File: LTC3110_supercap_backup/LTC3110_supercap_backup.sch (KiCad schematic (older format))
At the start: 28 parts

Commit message: Updated layout to include more net lables, ports, connectors
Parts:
- added P?: CONN_01X02, symbol CONN_01X02
- added P?: CONN_01X05, symbol CONN_01X05
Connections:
- net labels added: CAPOK, CAP_OK, DIR, FB, FBVCAP, MODE, RUN, VCAP, V_MID, V_SOLAR
- wire segments 87 -> 94
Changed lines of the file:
@@
 	4300 5250 4450 5250
 Wire Wire Line
-	2750 4700 2750 4650
+	2750 4650 2750 4700
 Wire Wire Line
 	3500 7200 7550 7200
@@
 $EndComp
 Wire Wire Line
-	8450 2650 8450 3150
-Wire Wire Line
-	8750 2900 8750 3150
-Wire Wire Line
 	8700 3150 8800 3150
 Connection ~ 8750 3150
@@
 	1    0    0    -1
 $EndComp
-Connection ~ 8450 2900
 $Comp
 L GND #PWR?
@@
 	1    0    0    -1
 $EndComp
-Wire Wire Line
-	8750 2900 11500 2900
 $Comp
 L C C?
@@
 	10650 4650 11300 4650
 Connection ~ 10700 2900
-Text GLabel 11500 2900 2    60   Input ~ 0
+Text GLabel 11300 2900 2    60   Input ~ 0
 V_SYS
 Text GLabel 11300 4650 2    60   Input ~ 0
 CAP_LOW
+Text GLabel 2500 4000 0    60   Input ~ 0
+V_SOLAR
+Wire Wire Line
+	2500 4000 2750 4000
+Connection ~ 2750 4000
+Text GLabel 2500 4650 0    60   Input ~ 0
+GND
+Wire Wire Line
+	2500 4650 2750 4650
+Text GLabel 11300 5200 2    60   Input ~ 0
+CAP_OK
+Connection ~ 9350 5200
+Wire Wire Line
+	11300 5200 9350 5200
+Wire Wire Line
+	8750 2900 11300 2900
+Wire Wire Line
+	8450 2650 8450 3150
+Connection ~ 8450 2900
+Wire Wire Line
+	8750 2900 8750 3150
+Text Label 5900 5250 0    60   ~ 0
+RUN
+Text Label 7350 7900 0    60   ~ 0
+MODE
+Text Label 9850 5200 0    60   ~ 0
+CAPOK
+Text Label 9250 4650 0    60   ~ 0
+DIR
+Text Label 9250 4300 0    60   ~ 0
+FB
+Text Label 6900 3150 0    60   ~ 0
+FBVCAP
+Text Label 5500 3650 0    60   ~ 0
+VCAP
+Text Label 5850 4800 0    60   ~ 0
+V_MID
+Text Label 2750 3550 0    60   ~ 0
+V_SOLAR
+$Comp
+L CONN_01X02 P?
+U 1 1 57C924FF
+P 1400 4300
+F 0 "P?" H 1400 4450 50  0000 C CNN
+F 1 "CONN_01X02" V 1500 4300 50  0000 C CNN
+F 2 "" H 1400 4300 50  0000 C CNN
+F 3 "" H 1400 4300 50  0000 C CNN
+	1    1400 4300
+	-1   0    0    -1
+$EndComp
+Connection ~ 2750 3850
+Wire Wire Line
+	1600 4350 2550 4350
+Wire Wire Line
+	2550 4350 2550 4650
+Connection ~ 2550 4650
+Wire Wire Line
+	1600 4250 1600 4100
+Wire Wire Line
+	1600 4100 2750 4100
+Connection ~ 2750 4100
+$Comp
+L CONN_01X05 P?
+U 1 1 57C92BCD
+P 13500 3800
+F 0 "P?" H 13500 4100 50  0000 C CNN
+F 1 "CONN_01X05" V 13600 3800 50  0000 C CNN
+F 2 "" H 13500 3800 50  0000 C CNN
+F 3 "" H 13500 3800 50  0000 C CNN
+	1    13500 3800
+	1    0    0    -1
+$EndComp
+Text GLabel 13300 3600 0    60   Input ~ 0
+V_SYS
+Text GLabel 13300 3700 0    60   Input ~ 0
+CAP_LOW
+Text GLabel 13300 3800 0    60   Input ~ 0
+CAP_OK
+Text GLabel 13300 4000 0    60   Input ~ 0
+GND
 $EndSCHEMATC

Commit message: Schematic tweaked and annotated, looking good, time for footprint matching and layout.
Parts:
- removed BT?: Solar Panel, symbol Battery
- removed P?: CONN_01X05, symbol CONN_01X05
- added P?: CONN_01X02, symbol CONN_01X02
- added P?: CONN_01X05, symbol CONN_01X05
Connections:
- net labels added: !CHRG
- wire segments 94 -> 99
- no-connect marks 4 -> 3
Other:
- note added: "Drawn by: Matthew Valancy\nBased on: LTC3110 datasheet page 32"
- moved on the sheet: P?
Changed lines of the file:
@@
-$EndComp
-$Comp
-L Battery BT?
-U 1 1 57C7BCD4
-P 2750 4500
-F 0 "BT?" H 2850 4550 50  0000 L CNN
-F 1 "Solar Panel" H 2850 4450 50  0000 L CNN
-F 2 "" V 2750 4540 50  0000 C CNN
-F 3 "" V 2750 4540 50  0000 C CNN
-	1    2750 4500
-	1    0    0    -1
 $EndComp
 $Comp
@@
 $EndComp
 Wire Wire Line
-	3050 4200 2750 4200
-Wire Wire Line
-	2750 3550 2750 4350
+	2750 4200 3050 4200
 Wire Wire Line
 	3500 4200 3350 4200
@@
 	4300 5250 4450 5250
 Wire Wire Line
-	2750 4650 2750 4700
+	2750 4400 2750 4700
 Wire Wire Line
 	3500 7200 7550 7200
@@
 	1    0    0    -1
 $EndComp
-NoConn ~ 9100 4900
 $Comp
 L R R?
@@
 L GND #PWR?
 U 1 1 57C8193E
-P 9750 5000
-F 0 "#PWR?" H 9750 4750 50  0001 C CNN
-F 1 "GND" H 9650 5050 50  0001 C CNN
-F 2 "" H 9750 5000 50  0000 C CNN
-F 3 "" H 9750 5000 50  0000 C CNN
-	1    9750 5000
-	1    0    0    -1
-$EndComp
-Wire Wire Line
-	9750 5000 9750 4950
+P 9750 4950
+F 0 "#PWR?" H 9750 4700 50  0001 C CNN
+F 1 "GND" H 9650 5000 50  0001 C CNN
+F 2 "" H 9750 4950 50  0000 C CNN
+F 3 "" H 9750 4950 50  0000 C CNN
+	1    9750 4950
+	1    0    0    -1
+$EndComp
 Wire Wire Line
 	10150 4650 10350 4650
@@
 Text Label 6900 3150 0    60   ~ 0
 FBVCAP
-Text Label 5500 3650 0    60   ~ 0
+Text Label 5650 3650 0    60   ~ 0
 VCAP
 Text Label 5850 4800 0    60   ~ 0
@@
 L CONN_01X02 P?
 U 1 1 57C924FF
-P 1400 4300
-F 0 "P?" H 1400 4450 50  0000 C CNN
-F 1 "CONN_01X02" V 1500 4300 50  0000 C CNN
-F 2 "" H 1400 4300 50  0000 C CNN
-F 3 "" H 1400 4300 50  0000 C CNN
-	1    1400 4300
+P 2150 4350
+F 0 "P?" H 2150 4500 50  0000 C CNN
+F 1 "CONN_01X02" V 2250 4350 50  0000 C CNN
+F 2 "" H 2150 4350 50  0000 C CNN
+F 3 "" H 2150 4350 50  0000 C CNN
+	1    2150 4350
 	-1   0    0    -1
 $EndComp
-Connection ~ 2750 3850
-Wire Wire Line
-	1600 4350 2550 4350
-Wire Wire Line
-	2550 4350 2550 4650
-Connection ~ 2550 4650
-Wire Wire Line
-	1600 4250 1600 4100
-Wire Wire Line
-	1600 4100 2750 4100
-Connection ~ 2750 4100
+Text GLabel 13300 3600 0    60   Input ~ 0
+V_SYS
+Text GLabel 13300 3800 0    60   Input ~ 0
+CAP_LOW
+Text GLabel 13300 3900 0    60   Input ~ 0
+CAP_OK
+Wire Wire Line
+	2750 3550 2750 4300
+Wire Wire Line
+	2750 4300 2350 4300
+Wire Wire Line
+	2350 4400 2750 4400
+Connection ~ 2750 4650
+Text GLabel 9100 4900 2    60   Input ~ 0
+!CHRG
+Text GLabel 13300 4000 0    60   Input ~ 0
+!CHRG
+Text GLabel 13300 3700 0    60   Input ~ 0
+GND
+$Comp
+L CONN_01X02 P?
+U 1 1 57C9525E
+P 4850 4150
+F 0 "P?" H 4850 4300 50  0000 C CNN
+F 1 "CONN_01X02" V 4950 4150 50  0000 C CNN
+F 2 "" H 4850 4150 50  0000 C CNN
+F 3 "" H 4850 4150 50  0000 C CNN
+	1    4850 4150
+	-1   0    0    -1
+$EndComp
+Wire Wire Line
+	5050 4100 5250 4100
+Wire Wire Line
+	5250 4100 5250 3800
+Wire Wire Line
+	5250 3800 5500 3800
+Connection ~ 5500 3800
+Wire Wire Line
+	5050 4200 5200 4200
+Wire Wire Line
+	5200 4200 5200 4650
+Wire Wire Line
+	5200 4650 5500 4650
+Connection ~ 5500 4650
+Wire Wire Line
+	9100 5100 10850 5100
+Wire Wire Line
+	10850 5100 10850 4650
+Connection ~ 10850 4650
 $Comp
 L CONN_01X05 P?
-U 1 1 57C92BCD
+U 1 1 57C961F0
 P 13500 3800
 F 0 "P?" H 13500 4100 50  0000 C CNN
@@
 	1    0    0    -1
 $EndComp
-Text GLabel 13300 3600 0    60   Input ~ 0
-V_SYS
-Text GLabel 13300 3700 0    60   Input ~ 0
-CAP_LOW
-Text GLabel 13300 3800 0    60   Input ~ 0
-CAP_OK
-Text GLabel 13300 4000 0    60   Input ~ 0
-GND
+Text Notes 12350 9500 0    60   ~ 0
+Drawn by: Matthew Valancy\nBased on: LTC3110 datasheet page 32
 $EndSCHEMATC

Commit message: saved project
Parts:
- gave numbers to parts that had none: 30

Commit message: Selected critical components for LTC3110 breakout, associated footprints and added necessary footprints to library, output netlist and started layout
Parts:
- removed U1: LTC2935-2, symbol LTC2935-2
- added U1: LTC2935-2-TS8, TO_SOT_Packages_SMD:SOT-23, symbol LTC2935-2-TS8
- C1, C2: footprint (none) -> MRV_TH_Passives:Cap_HB1860; MFG_PN (none) -> HB1860-2R5117-R
- C3, C4, C5, C6: footprint (none) -> Capacitors_SMD:C_0805_HandSoldering
- C7, C8: footprint (none) -> Capacitors_ThroughHole:C_Rect_L32_W15_P27; MFG_PN (none) -> UHW1E472MHD
- L1: footprint (none) -> MRV_SMD_Passives:SMD_IND_CLF7045; MFG_PN (none) -> CLF7045T-2R2N-D
- M1, M2: footprint (none) -> TO_SOT_Packages_SMD:SOT-23
- P1, P2: footprint (none) -> Pin_Headers:Pin_Header_Straight_1x02
- P3: footprint (none) -> Pin_Headers:Pin_Header_Straight_1x05
- Q1: footprint (none) -> TO_SOT_Packages_SMD:SOT-223; MFG_PN (none) -> PBSS302
- R1, R10, R11, R12, R13, R4, R5, R6, R7, R8, R9: footprint (none) -> Resistors_SMD:R_0805_HandSoldering
- R2: footprint (none) -> Resistors_SMD:R_0805_HandSoldering; MFG_PN (none) -> ERJ-6ENF1914V
- R3: footprint (none) -> Resistors_SMD:R_0805_HandSoldering; MFG_PN (none) -> CRCW0805523KFKEA
- U2: footprint (none) -> MRV_SMD_Packages:TSSOP-24

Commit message: Layout almost complete
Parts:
- U1: footprint TO_SOT_Packages_SMD:SOT-23 -> MRV_SMD_Packages:TSOT-23-8
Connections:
- wire segments 99 -> 102
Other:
- moved on the sheet: C3
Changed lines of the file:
@@
 LIBS:contrib
 LIBS:valves
-LIBS:ICs_PM
-LIBS:MF_Aesthetics
-LIBS:MF_Connectors
-LIBS:MF_Discrete_Semiconductor
-LIBS:MF_Displays
-LIBS:MF_Frequency_Control
-LIBS:MF_IC_Analog
-LIBS:MF_IC_Digital
-LIBS:MF_IC_Power
-LIBS:MF_LEDs
-LIBS:MF_Passives
-LIBS:MF_Sensors
-LIBS:MF_Switches
 LIBS:LTC3110_supercap_backup-cache
 EELAYER 25 0
@@
 L C C3
 U 1 1 57C7F46D
-P 6650 3800
-F 0 "C3" H 6675 3900 50  0000 L CNN
-F 1 "47uF" H 6675 3700 50  0000 L CNN
-F 2 "Capacitors_SMD:C_0805_HandSoldering" H 6688 3650 50  0001 C CNN
-F 3 "" H 6650 3800 50  0000 C CNN
-	1    6650 3800
+P 6650 3850
+F 0 "C3" H 6675 3950 50  0000 L CNN
+F 1 "47uF" H 6675 3750 50  0000 L CNN
+F 2 "Capacitors_SMD:C_0805_HandSoldering" H 6688 3700 50  0001 C CNN
+F 3 "" H 6650 3850 50  0000 C CNN
+	1    6650 3850
 	1    0    0    -1
 $EndComp
@@
 L GND #PWR013
 U 1 1 57C7F4EE
-P 6650 4000
-F 0 "#PWR013" H 6650 3750 50  0001 C CNN
-F 1 "GND" H 6550 4050 50  0001 C CNN
-F 2 "" H 6650 4000 50  0000 C CNN
-F 3 "" H 6650 4000 50  0000 C CNN
-	1    6650 4000
-	1    0    0    -1
-$EndComp
-Wire Wire Line
-	6650 4000 6650 3950
+P 6650 4050
+F 0 "#PWR013" H 6650 3800 50  0001 C CNN
+F 1 "GND" H 6550 4100 50  0001 C CNN
+F 2 "" H 6650 4050 50  0000 C CNN
+F 3 "" H 6650 4050 50  0000 C CNN
+	1    6650 4050
+	1    0    0    -1
+$EndComp
 $Comp
 L L_Small L1
@@
 	9750 3750 10250 3750
 Connection ~ 10250 4650
-Wire Wire Line
-	9800 2150 9800 3750
 Connection ~ 9800 2900
 Wire Wire Line
@@
 F 0 "U1" H 4750 7200 60  0000 C CNN
 F 1 "LTC2935-2-TS8" H 5050 7100 60  0000 C CNN
-F 2 "TO_SOT_Packages_SMD:SOT-23" H 4450 6100 60  0001 C CNN
+F 2 "MRV_SMD_Packages:TSOT-23-8" H 4450 6100 60  0001 C CNN
 F 3 "" H 4450 6100 60  0001 C CNN
 	1    4450 6000
 	1    0    0    -1
 $EndComp
+Wire Wire Line
+	8300 5500 8450 5500
+Wire Wire Line
+	7900 5650 8100 5650
+Wire Wire Line
+	6650 4050 6650 4000
+Wire Wire Line
+	6650 3700 6650 3650
+Connection ~ 6650 3650
+Wire Wire Line
+	9800 3750 9800 2900
+Connection ~ 9800 3750
 $EndSCHEMATC

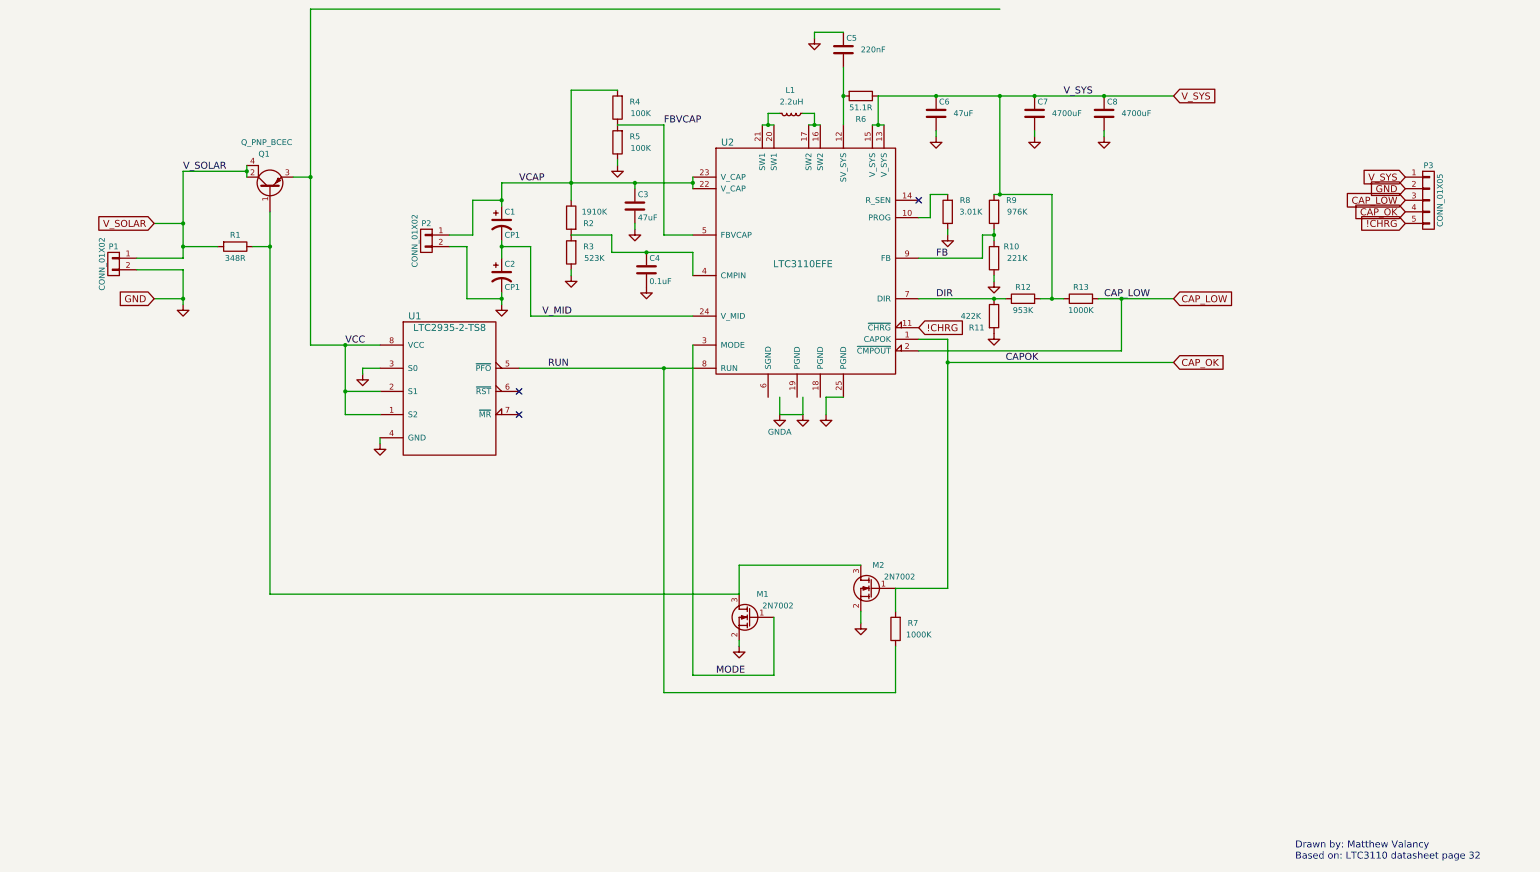
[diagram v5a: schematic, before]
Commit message: re-routed CAP_OK to avoid major ground plane division
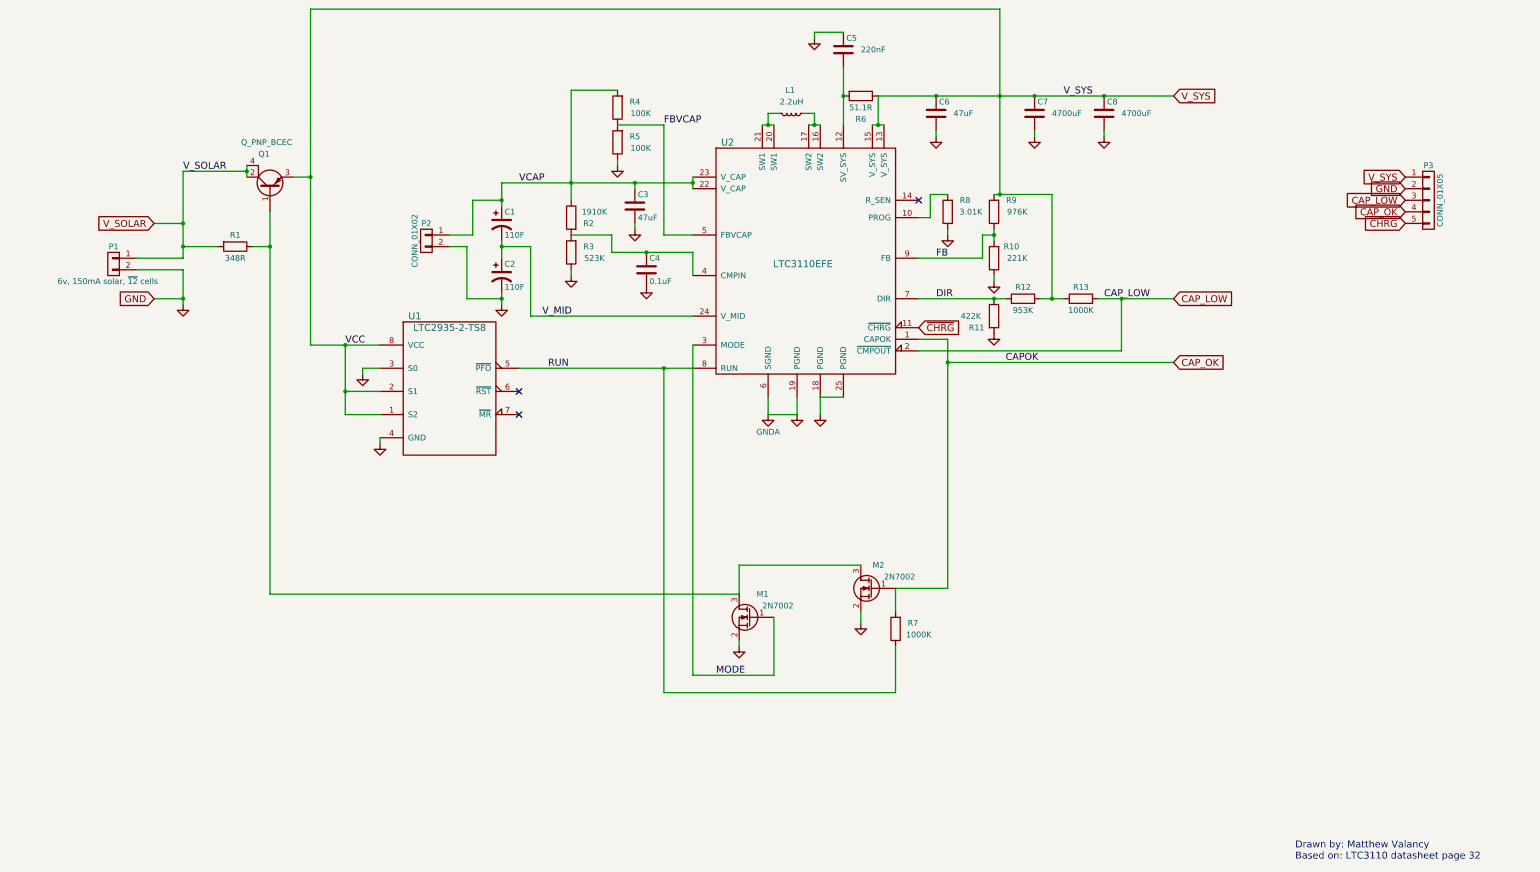
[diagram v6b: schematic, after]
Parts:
- C1, C2: value CP1 -> 110F
- P1: value CONN_01X02 -> 6v, 150mA solar, ~12 cells
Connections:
- net VCC is gone; now on net V_SYS: Q1.3 (E), U1.1 (S2), U1.2 (S1), U1.8 (VCC)
- net GND: now also U2.18 (PGND), U2.19 (PGND), U2.6 (SGND)
- net !CHRG renamed ~CHRG
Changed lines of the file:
@@
 LIBS:contrib
 LIBS:valves
+LIBS:MRV_ICs_PM
 LIBS:LTC3110_supercap_backup-cache
 EELAYER 25 0
@@
 L GNDA #PWR06
 U 1 1 57C7DBE5
-P 7900 5650
-F 0 "#PWR06" H 7900 5400 50  0001 C CNN
-F 1 "GNDA" H 7900 5500 50  0000 C CNN
-F 2 "" H 7900 5650 50  0000 C CNN
-F 3 "" H 7900 5650 50  0000 C CNN
-	1    7900 5650
+P 7800 5650
+F 0 "#PWR06" H 7800 5400 50  0001 C CNN
+F 1 "GNDA" H 7800 5500 50  0000 C CNN
+F 2 "" H 7800 5650 50  0000 C CNN
+F 3 "" H 7800 5650 50  0000 C CNN
+	1    7800 5650
 	1    0    0    -1
 $EndComp
@@
 L GND #PWR07
 U 1 1 57C7DC74
-P 8100 5650
-F 0 "#PWR07" H 8100 5400 50  0001 C CNN
-F 1 "GND" H 8000 5700 50  0001 C CNN
-F 2 "" H 8100 5650 50  0000 C CNN
-F 3 "" H 8100 5650 50  0000 C CNN
-	1    8100 5650
+P 8050 5650
+F 0 "#PWR07" H 8050 5400 50  0001 C CNN
+F 1 "GND" H 7950 5700 50  0001 C CNN
+F 2 "" H 8050 5650 50  0000 C CNN
+F 3 "" H 8050 5650 50  0000 C CNN
+	1    8050 5650
 	1    0    0    -1
 $EndComp
@@
 L GND #PWR08
 U 1 1 57C7DCF0
-P 8300 5650
-F 0 "#PWR08" H 8300 5400 50  0001 C CNN
-F 1 "GND" H 8200 5700 50  0001 C CNN
-F 2 "" H 8300 5650 50  0000 C CNN
-F 3 "" H 8300 5650 50  0000 C CNN
-	1    8300 5650
+P 8250 5650
+F 0 "#PWR08" H 8250 5400 50  0001 C CNN
+F 1 "GND" H 8150 5700 50  0001 C CNN
+F 2 "" H 8250 5650 50  0000 C CNN
+F 3 "" H 8250 5650 50  0000 C CNN
+	1    8250 5650
 	1    0    0    -1
 $EndComp
@@
 P 5500 4000
 F 0 "C1" H 5525 4100 50  0000 L CNN
-F 1 "CP1" H 5525 3900 50  0000 L CNN
+F 1 "110F" H 5525 3900 50  0000 L CNN
 F 2 "MRV_TH_Passives:Cap_HB1860" H 5500 4000 50  0001 C CNN
 F 3 "" H 5500 4000 50  0000 C CNN
@@
 P 5500 4450
 F 0 "C2" H 5525 4550 50  0000 L CNN
-F 1 "CP1" H 5525 4350 50  0000 L CNN
+F 1 "110F" H 5525 4350 50  0000 L CNN
 F 2 "MRV_TH_Passives:Cap_HB1860" H 5500 4450 50  0001 C CNN
 F 3 "" H 5500 4450 50  0000 C CNN
@@
 	3500 4200 3350 4200
 Wire Wire Line
-	3300 3500 3300 3600
+	3300 3500 3300 3550
+Wire Wire Line
+	3300 3550 3300 3600
 Wire Wire Line
 	2750 3550 3300 3550
@@
 	3700 3600 3850 3600
 Wire Wire Line
-	3850 2150 3850 5050
-Wire Wire Line
-	3850 5050 4450 5050
+	3850 2150 3850 3600
+Wire Wire Line
+	3850 3600 3850 5050
+Wire Wire Line
+	3850 5050 4150 5050
+Wire Wire Line
+	4150 5050 4450 5050
 Wire Wire Line
 	4300 5250 4450 5250
 Wire Wire Line
-	2750 4400 2750 4700
+	2750 4400 2750 4650
+Wire Wire Line
+	2750 4650 2750 4700
 Wire Wire Line
 	3500 7200 7550 7200
 Connection ~ 3500 4200
 Wire Wire Line
-	4150 5050 4150 5650
+	4150 5050 4150 5450
+Wire Wire Line
+	4150 5450 4150 5650
 Wire Wire Line
 	4150 5450 4450 5450
@@
 	7550 6950 8600 6950
 Wire Wire Line
-	7150 5250 5650 5250
-Wire Wire Line
-	3500 7200 3500 3900
+	7150 5250 6900 5250
+Wire Wire Line
+	6900 5250 5650 5250
+Wire Wire Line
+	3500 7200 3500 4200
+Wire Wire Line
+	3500 4200 3500 3900
 Wire Wire Line
 	7550 7650 7550 7600
@@
 	8600 7450 8600 7350
 Wire Wire Line
-	7900 5650 7900 5500
-Wire Wire Line
-	8100 5650 8100 5500
-Wire Wire Line
-	8300 5650 8300 5500
-Wire Wire Line
-	5500 3850 5500 3650
-Wire Wire Line
-	5500 3650 7150 3650
-Wire Wire Line
-	7150 3600 7150 3700
+	7800 5650 7800 5500
+Wire Wire Line
+	8050 5650 8050 5500
+Wire Wire Line
+	8250 5650 8250 5500
+Wire Wire Line
+	5500 3850 5500 3800
+Wire Wire Line
+	5500 3800 5500 3650
+Wire Wire Line
+	5500 3650 6100 3650
+Wire Wire Line
+	6100 3650 6650 3650
+Wire Wire Line
+	6650 3650 7150 3650
+Wire Wire Line
+	7150 3600 7150 3650
+Wire Wire Line
+	7150 3650 7150 3700
 Connection ~ 7150 3650
 Wire Wire Line
-	5500 4150 5500 4300
-Wire Wire Line
-	5500 4700 5500 4600
+	5500 4150 5500 4200
+Wire Wire Line
+	5500 4200 5500 4300
+Wire Wire Line
+	5500 4700 5500 4650
+Wire Wire Line
+	5500 4650 5500 4600
 Wire Wire Line
 	7150 4800 5750 4800
@@
 	7150 4250 7150 4450
 Wire Wire Line
-	6450 4250 7150 4250
+	6450 4250 6750 4250
+Wire Wire Line
+	6750 4250 7150 4250
 Wire Wire Line
 	6450 4250 6450 4100
@@
 Connection ~ 6750 4250
 Wire Wire Line
-	6100 2850 6100 3800
+	6100 2850 6100 3650
+Wire Wire Line
+	6100 3650 6100 3800
 Connection ~ 6100 3650
 $Comp
@@
 	7800 3050 7800 3150
 Wire Wire Line
-	7750 3150 7850 3150
+	7750 3150 7800 3150
+Wire Wire Line
+	7800 3150 7850 3150
 Connection ~ 7800 3150
 Wire Wire Line
@@
 	8200 3050 8200 3150
 Wire Wire Line
-	8150 3150 8250 3150
+	8150 3150 8200 3150
+Wire Wire Line
+	8200 3150 8250 3150
 Connection ~ 8200 3150
 $Comp
@@
 $EndComp
 Wire Wire Line
-	8700 3150 8800 3150
+	8700 3150 8750 3150
+Wire Wire Line
+	8750 3150 8800 3150
 Connection ~ 8750 3150
 $Comp
@@
 	9650 4100 9750 4100
 Wire Wire Line
-	9750 4050 9750 4150
+	9750 4050 9750 4100
+Wire Wire Line
+	9750 4100 9750 4150
 Connection ~ 9750 4100
 $Comp
@@
 	9100 5000 9350 5000
 Wire Wire Line
-	9350 5000 9350 7150
+	9350 5000 9350 5200
+Wire Wire Line
+	9350 5200 9350 7150
 Wire Wire Line
 	9350 7150 8900 7150
 Wire Wire Line
-	9100 4650 9850 4650
+	9100 4650 9750 4650
+Wire Wire Line
+	9750 4650 9850 4650
 Connection ~ 9750 4650
 $Comp
@@
 $EndComp
 Wire Wire Line
-	10150 4650 10350 4650
+	10150 4650 10250 4650
+Wire Wire Line
+	10250 4650 10350 4650
 Wire Wire Line
 	10250 3750 10250 4650
 Wire Wire Line
-	9750 3750 10250 3750
+	9750 3750 9800 3750
+Wire Wire Line
+	9800 3750 10250 3750
 Connection ~ 10250 4650
 Connection ~ 9800 2900
@@
 CAP_LOW
 Wire Wire Line
-	10650 4650 11300 4650
+	10650 4650 10850 4650
+Wire Wire Line
+	10850 4650 11300 4650
 Connection ~ 10700 2900
 Text GLabel 11300 2900 2    60   Input ~ 0
@@
 	11300 5200 9350 5200
 Wire Wire Line
-	8750 2900 11300 2900
-Wire Wire Line
-	8450 2650 8450 3150
+	8750 2900 9250 2900
+Wire Wire Line
+	9250 2900 9800 2900
+Wire Wire Line
+	9800 2900 10100 2900
+Wire Wire Line
+	10100 2900 10700 2900
+Wire Wire Line
+	10700 2900 11300 2900
+Wire Wire Line
+	8450 2650 8450 2900
+Wire Wire Line
+	8450 2900 8450 3150
 Connection ~ 8450 2900
 Wire Wire Line
@@
 P 2150 4350
 F 0 "P1" H 2150 4500 50  0000 C CNN
-F 1 "CONN_01X02" V 2250 4350 50  0000 C CNN
+F 1 "6v, 150mA solar, ~12 cells" H 2200 4200 50  0000 C CNN
 F 2 "Pin_Headers:Pin_Header_Straight_1x02" H 2150 4350 50  0001 C CNN
 F 3 "" H 2150 4350 50  0000 C CNN
@@
 CAP_OK
 Wire Wire Line
-	2750 3550 2750 4300
+	2750 3550 2750 4000
+Wire Wire Line
+	2750 4000 2750 4200
+Wire Wire Line
+	2750 4200 2750 4300
 Wire Wire Line
 	2750 4300 2350 4300
@@
 Connection ~ 2750 4650
 Text GLabel 9100 4900 2    60   Input ~ 0
-!CHRG
+~CHRG
 Text GLabel 13300 4000 0    60   Input ~ 0
-!CHRG
+~CHRG
 Text GLabel 13300 3700 0    60   Input ~ 0
 GND
@@
 $EndComp
 Wire Wire Line
-	8300 5500 8450 5500
-Wire Wire Line
-	7900 5650 8100 5650
+	8250 5500 8450 5500
+Wire Wire Line
+	7800 5650 8050 5650
 Wire Wire Line
 	6650 4050 6650 4000
@@
 Connection ~ 6650 3650
 Wire Wire Line
-	9800 3750 9800 2900
+	9800 2150 9800 2900
+Wire Wire Line
+	9800 2900 9800 3750
 Connection ~ 9800 3750
 $EndSCHEMATC
